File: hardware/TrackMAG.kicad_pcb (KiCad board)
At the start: 4 copper layers, 36 x 36 mm, 54 parts, among them J1 USB_C_Socket_USB2.0, J2 Conn_Debug, SW1 SW_RESET, SW2 SW_BOOT, U1 LSM6DS3TR-C, U2 USBLC6-2P6, U3 STM32F103C8T6, U4 LIS2MDL, U5 AMS1117-3.3, Y1 16MHz

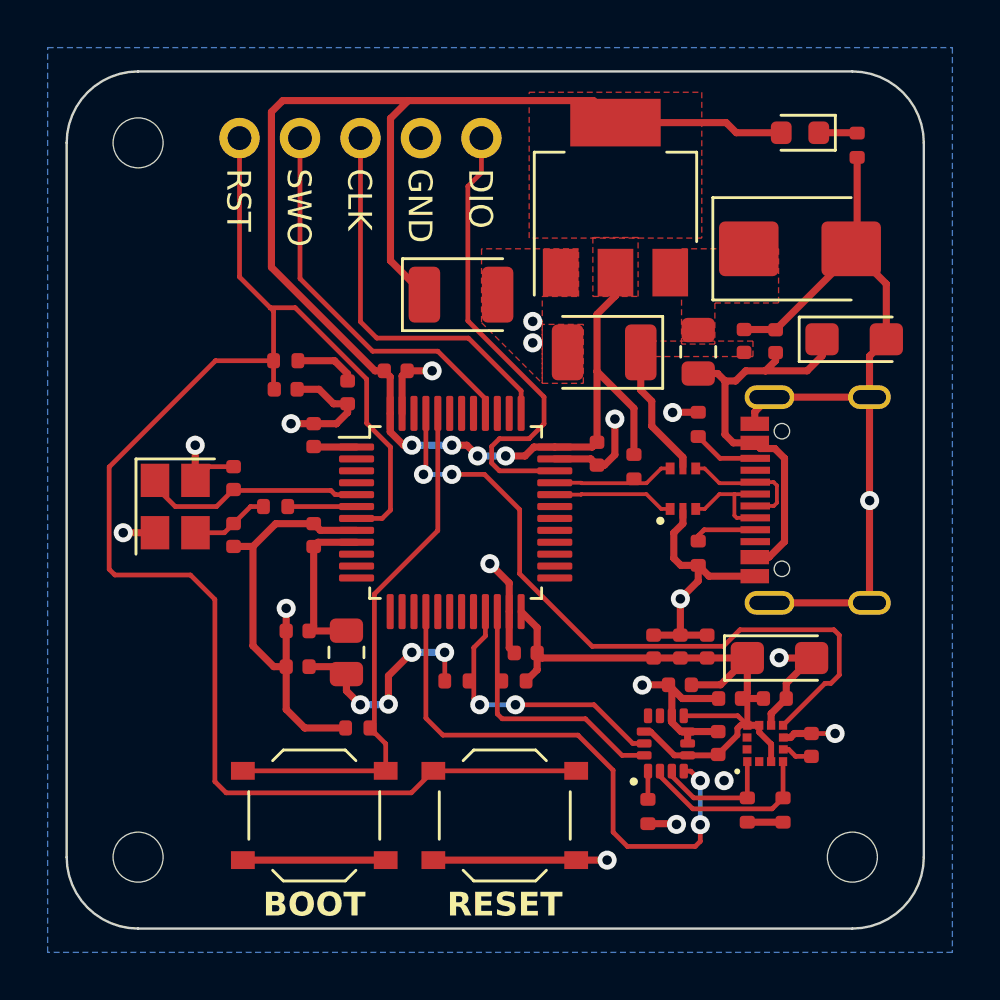
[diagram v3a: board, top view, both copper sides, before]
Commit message: Add ground planes
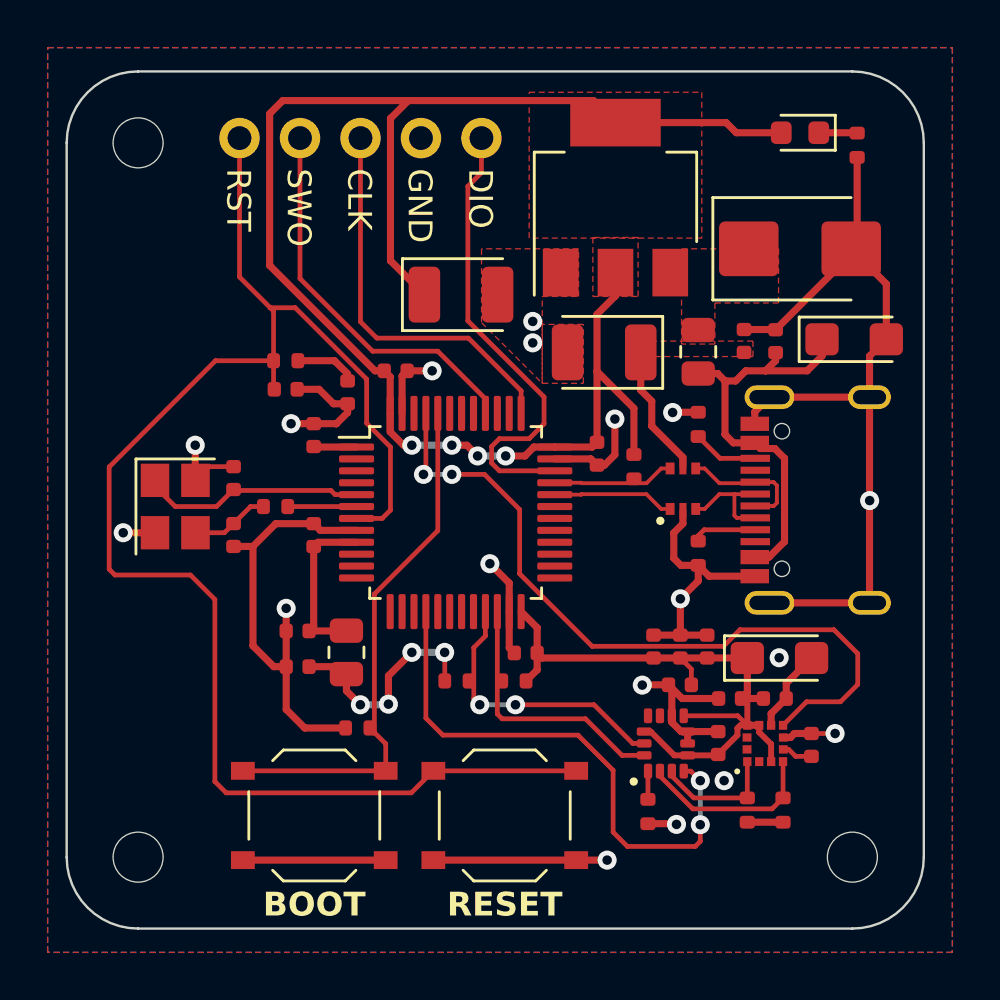
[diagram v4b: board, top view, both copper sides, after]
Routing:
- net +3.3V: track 120.2 -> 118.7 mm
- net GND: track 112.0 -> 110.6 mm
- net DRDY: track 29.9 -> 31.3 mm
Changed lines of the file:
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@@
   (segment (start 51.4 39.95) (end 51.4 33.975) (width 0.3) (layer "F.Cu") (net 1))
   (segment (start 62.45 56.635) (end 57.77 56.635) (width 0.3) (layer "F.Cu") (net 1))
-  (segment (start 46.4 40.225) (end 46.4 33.7) (width 0.3) (layer "F.Cu") (net 1))
-  (segment (start 51.14 44.575) (end 50.75 44.575) (width 0.3) (layer "F.Cu") (net 1))
+  (segment (start 50.75 44.575) (end 51.14 44.575) (width 0.3) (layer "F.Cu") (net 1))
+  (segment (start 64.0375 57.0975) (end 63.575 56.635) (width 0.2) (layer "F.Cu") (net 1))
   (segment (start 49.05 44.15) (end 47.51 44.15) (width 0.3) (layer "F.Cu") (net 1))
   (segment (start 51.3875 44.8225) (end 51.14 44.575) (width 0.3) (layer "F.Cu") (net 1))
@@
   (segment (start 66.095 59.4625) (end 66.3875 59.4625) (width 0.25) (layer "F.Cu") (net 1))
   (segment (start 53.68 57.6) (end 53.68 56.405) (width 0.2) (layer "F.Cu") (net 1))
-  (segment (start 46.875 33.225) (end 52.15 33.225) (width 0.3) (layer "F.Cu") (net 1))
+  (segment (start 52.15 33.225) (end 46.875 33.225) (width 0.3) (layer "F.Cu") (net 1))
   (segment (start 65.9875 59.0625) (end 66.3875 59.4625) (width 0.2) (layer "F.Cu") (net 1))
   (segment (start 58.3 47.775) (end 57.425 47.775) (width 0.3) (layer "F.Cu") (net 1))
   (segment (start 61.625 46.15) (end 60.075 44.6) (width 0.3) (layer "F.Cu") (net 1))
+  (segment (start 46.325 33.775) (end 46.325 40.15) (width 0.3) (layer "F.Cu") (net 1))
   (segment (start 63.325 60.725) (end 63.88 60.725) (width 0.25) (layer "F.Cu") (net 1))
   (segment (start 55.0605 48.15) (end 54.609841 47.699341) (width 0.3) (layer "F.Cu") (net 1))
@@
   (segment (start 52.296271 47.699305) (end 52.196966 47.6) (width 0.3) (layer "F.Cu") (net 1))
   (segment (start 59.875 47.775) (end 60.075 47.575) (width 0.3) (layer "F.Cu") (net 1))
-  (segment (start 50.75 44.575) (end 46.4 40.225) (width 0.3) (layer "F.Cu") (net 1))
   (segment (start 66.3875 63.5325) (end 67.8875 63.5325) (width 0.3) (layer "F.Cu") (net 1))
   (segment (start 57.56 55.36) (end 56.8875 54.6875) (width 0.3) (layer "F.Cu") (net 1))
@@
   (segment (start 60.075 42.2) (end 60.075 44.6) (width 0.3) (layer "F.Cu") (net 1))
   (segment (start 53.68 56.405) (end 53.675 56.4) (width 0.2) (layer "F.Cu") (net 1))
-  (segment (start 64.0375 57.7625) (end 65.2625 57.7625) (width 0.3) (layer "F.Cu") (net 1))
   (segment (start 57.56 56.425) (end 57.56 57.135) (width 0.3) (layer "F.Cu") (net 1))
   (segment (start 52.825 41.375) (end 51.4 39.95) (width 0.3) (layer "F.Cu") (net 1))
@@
   (segment (start 51.3145 57.3835) (end 52.298 56.4) (width 0.3) (layer "F.Cu") (net 1))
   (segment (start 60.075 44.6) (end 60.075 47.575) (width 0.3) (layer "F.Cu") (net 1))
-  (segment (start 46.4 33.7) (end 46.875 33.225) (width 0.3) (layer "F.Cu") (net 1))
+  (segment (start 64.0375 57.7625) (end 64.0375 57.0975) (width 0.2) (layer "F.Cu") (net 1))
   (segment (start 62.055 59.725) (end 62.325 59.725) (width 0.25) (layer "F.Cu") (net 1))
   (segment (start 48.195 47.775) (end 48.175 47.755) (width 0.3) (layer "F.Cu") (net 1))
   (segment (start 66.3875 59.4625) (end 66.8875 59.4625) (width 0.3) (layer "F.Cu") (net 1))
+  (segment (start 46.875 33.225) (end 46.325 33.775) (width 0.3) (layer "F.Cu") (net 1))
   (segment (start 52.15 33.225) (end 59.925 33.225) (width 0.3) (layer "F.Cu") (net 1))
   (segment (start 63.7175 59.0625) (end 65.9875 59.0625) (width 0.2) (layer "F.Cu") (net 1))
@@
   (segment (start 60.85 40.45) (end 60.85 41.425) (width 0.3) (layer "F.Cu") (net 1))
   (segment (start 57.425 47.775) (end 57.05 48.15) (width 0.3) (layer "F.Cu") (net 1))
+  (segment (start 46.325 40.15) (end 50.75 44.575) (width 0.3) (layer "F.Cu") (net 1))
   (segment (start 49.55 58.0145) (end 50.1355 58.6) (width 0.3) (layer "F.Cu") (net 1))
   (segment (start 57.05 48.15) (end 56.2395 48.15) (width 0.3) (layer "F.Cu") (net 1))
-  (segment (start 65.2625 57.7625) (end 66.3875 56.6375) (width 0.3) (layer "F.Cu") (net 1))
   (segment (start 57.56 56.425) (end 57.56 55.36) (width 0.3) (layer "F.Cu") (net 1))
   (segment (start 49.2375 57) (end 49.55 57.3125) (width 0.3) (layer "F.Cu") (net 1))
@@
   (segment (start 71.52 45.68) (end 71.52 50.02) (width 0.3) (layer "F.Cu") (net 2))
   (segment (start 48.455 51.275) (end 48.175 50.995) (width 0.3) (layer "F.Cu") (net 2))
-  (segment (start 69.0875 56.6375) (end 67.7375 56.6375) (width 0.3) (layer "F.Cu") (net 2))
   (segment (start 66.7 46.8) (end 66.7 46.3) (width 0.3) (layer "F.Cu") (net 2))
   (segment (start 64.325 46.315) (end 63.26 46.315) (width 0.3) (layer "F.Cu") (net 2))
@@
   (segment (start 62.149999 49.755) (end 59.426251 49.755) (width 0.16) (layer "F.Cu") (net 22))
   (segment (start 59.406251 49.775) (end 58.3 49.775) (width 0.16) (layer "F.Cu") (net 22))
-  (segment (start 66.077746 55.45) (end 70.025 55.45) (width 0.2) (layer "F.Cu") (net 46))
-  (segment (start 69.65 57.7) (end 67.8875 59.4625) (width 0.2) (layer "F.Cu") (net 46))
+  (segment (start 55.35 48.925) (end 53.977 48.925) (width 0.2) (layer "F.Cu") (net 46))
+  (segment (start 70.025 55.45) (end 66.077746 55.45) (width 0.2) (layer "F.Cu") (net 46))
+  (segment (start 71.025 56.45) (end 70.025 55.45) (width 0.2) (layer "F.Cu") (net 46))
   (segment (start 52.8875 46.3625) (end 52.8875 48.823) (width 0.2) (layer "F.Cu") (net 46))
-  (segment (start 59.87 56.145) (end 65.382746 56.145) (width 0.2) (layer "F.Cu") (net 46))
-  (segment (start 65.382746 56.145) (end 66.077746 55.45) (width 0.2) (layer "F.Cu") (net 46))
-  (segment (start 56.825 50.4) (end 56.825 53.1) (width 0.2) (layer "F.Cu") (net 46))
-  (segment (start 70.25 55.675) (end 70.25 57.35) (width 0.2) (layer "F.Cu") (net 46))
+  (segment (start 56.825 50.4) (end 55.35 48.925) (width 0.2) (layer "F.Cu") (net 46))
+  (segment (start 67.8875 59.4625) (end 68.875 58.475) (width 0.2) (layer "F.Cu") (net 46))
+  (segment (start 66.077746 55.45) (end 65.382746 56.145) (width 0.2) (layer "F.Cu") (net 46))
+  (segment (start 59.87 56.145) (end 56.825 53.1) (width 0.2) (layer "F.Cu") (net 46))
+  (segment (start 70.3 58.475) (end 71.025 57.75) (width 0.2) (layer "F.Cu") (net 46))
+  (segment (start 65.382746 56.145) (end 59.87 56.145) (width 0.2) (layer "F.Cu") (net 46))
   (segment (start 52.8875 48.823) (end 52.7855 48.925) (width 0.2) (layer "F.Cu") (net 46))
-  (segment (start 69.9 57.7) (end 69.65 57.7) (width 0.2) (layer "F.Cu") (net 46))
-  (segment (start 70.025 55.45) (end 70.25 55.675) (width 0.2) (layer "F.Cu") (net 46))
-  (segment (start 53.977 48.925) (end 55.35 48.925) (width 0.2) (layer "F.Cu") (net 46))
-  (segment (start 70.25 57.35) (end 69.9 57.7) (width 0.2) (layer "F.Cu") (net 46))
-  (segment (start 55.35 48.925) (end 56.825 50.4) (width 0.2) (layer "F.Cu") (net 46))
-  (segment (start 56.825 53.1) (end 59.87 56.145) (width 0.2) (layer "F.Cu") (net 46))
+  (segment (start 56.825 53.1) (end 56.825 50.4) (width 0.2) (layer "F.Cu") (net 46))
+  (segment (start 71.025 57.75) (end 71.025 56.45) (width 0.2) (layer "F.Cu") (net 46))
+  (segment (start 68.875 58.475) (end 70.3 58.475) (width 0.2) (layer "F.Cu") (net 46))
   (via (at 52.7855 48.925) (size 0.8) (drill 0.4) (layers "F.Cu" "B.Cu") (net 46))
   (via (at 53.977 48.925) (size 0.8) (drill 0.4) (layers "F.Cu" "B.Cu") (net 46))
@@
       )
     )
+  )
+  (zone (net 2) (net_name "GND") (layer "F.Cu") (hatch edge 0.5)
+    (priority 1)
+    (connect_pads thru_hole_only (clearance 0.5))
+    (min_thickness 0.3) (filled_areas_thickness no)
+    (fill yes (thermal_gap 0.3) (thermal_bridge_width 0.3))
+    (polygon
+      (pts
+        (xy 37 31)
+        (xy 75 31)
+        (xy 75 69)
+        (xy 37 69)
+      )
+    )

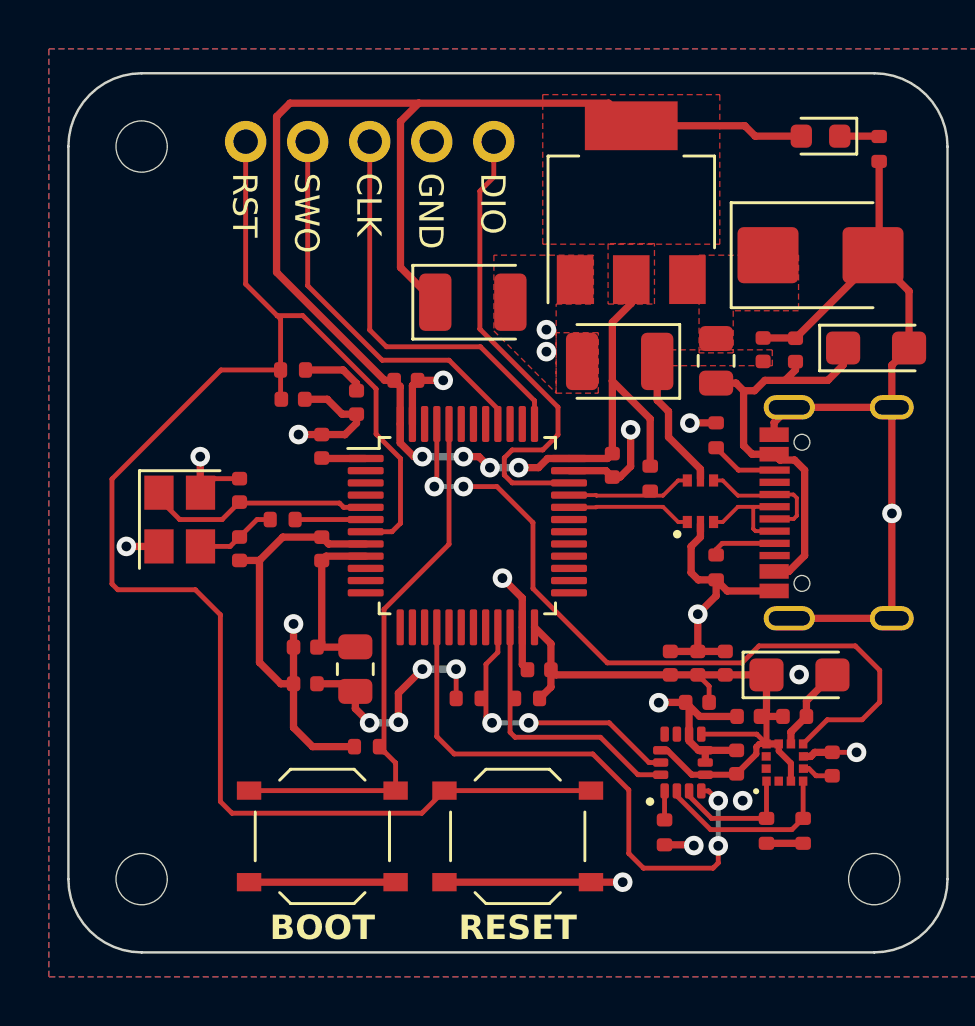
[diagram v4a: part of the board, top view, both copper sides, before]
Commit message: Add missing connections
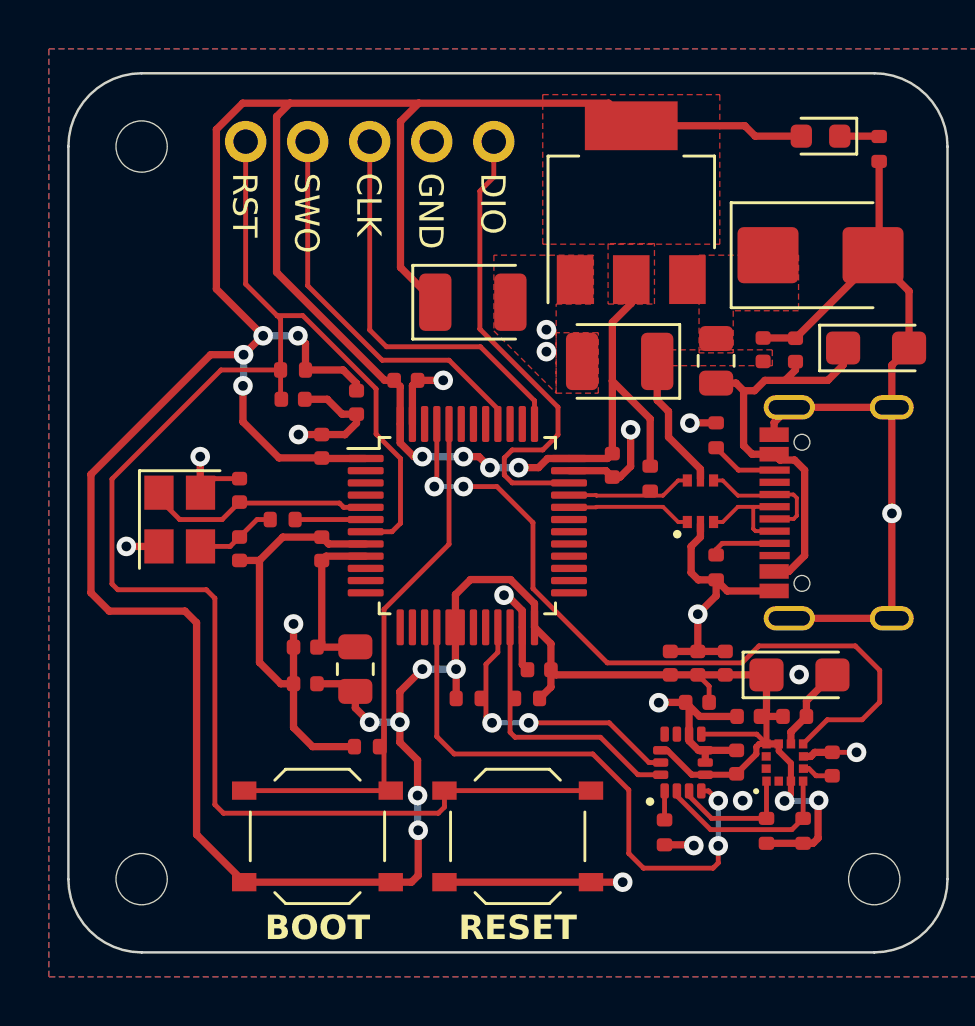
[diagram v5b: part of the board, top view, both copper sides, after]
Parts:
- moved SW2 0.20 mm to (48.0, 63.2)
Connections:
- U3 pad 17: unconnected-(U3-PA7-Pad17) -> +3.3V
- U3 pad 18: unconnected-(U3-PB0-Pad18) -> +3.3V
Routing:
- net +3.3V: track 118.7 -> 191.9 mm, vias 8 -> 16
- net /BOOT0: track 22.6 -> 23.5 mm
- net RESET: track 65.3 -> 66.2 mm
- net GND: track 110.6 -> 110.0 mm

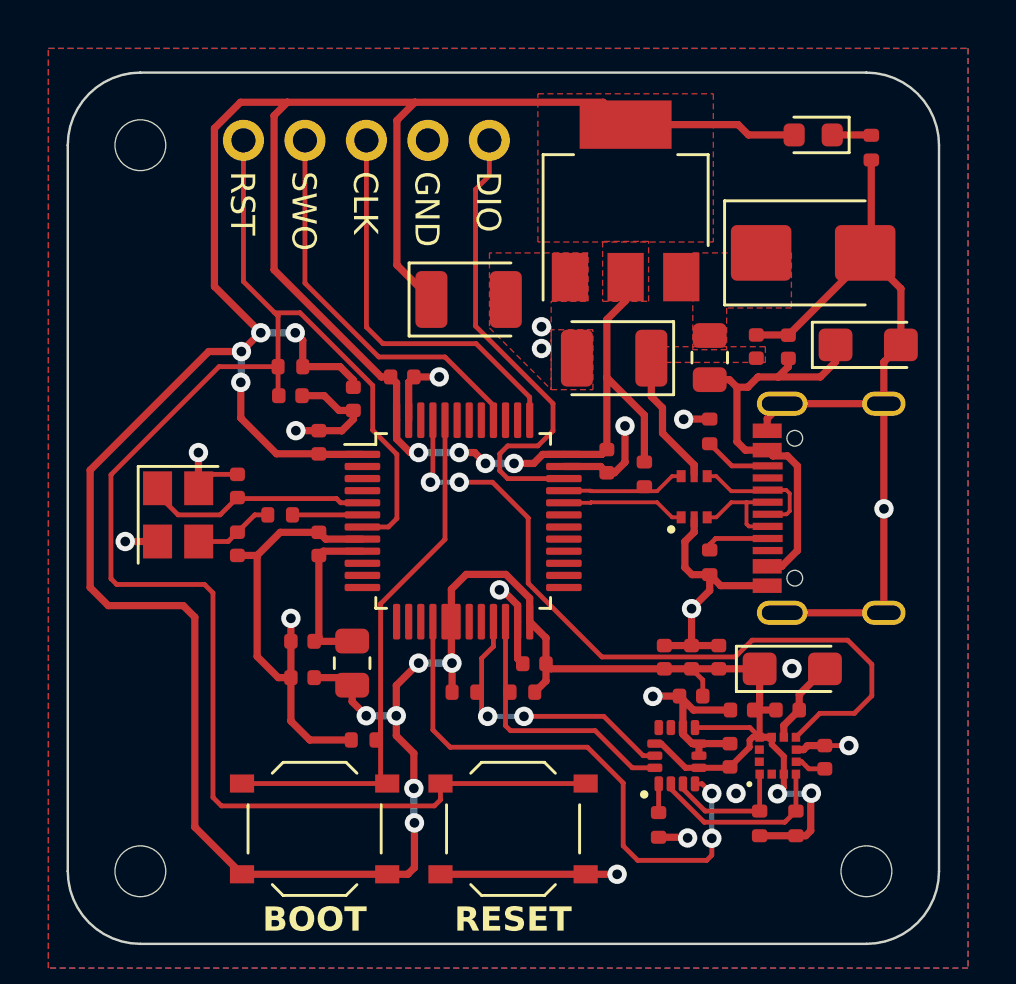
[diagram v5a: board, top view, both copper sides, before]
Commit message: Add reference vias
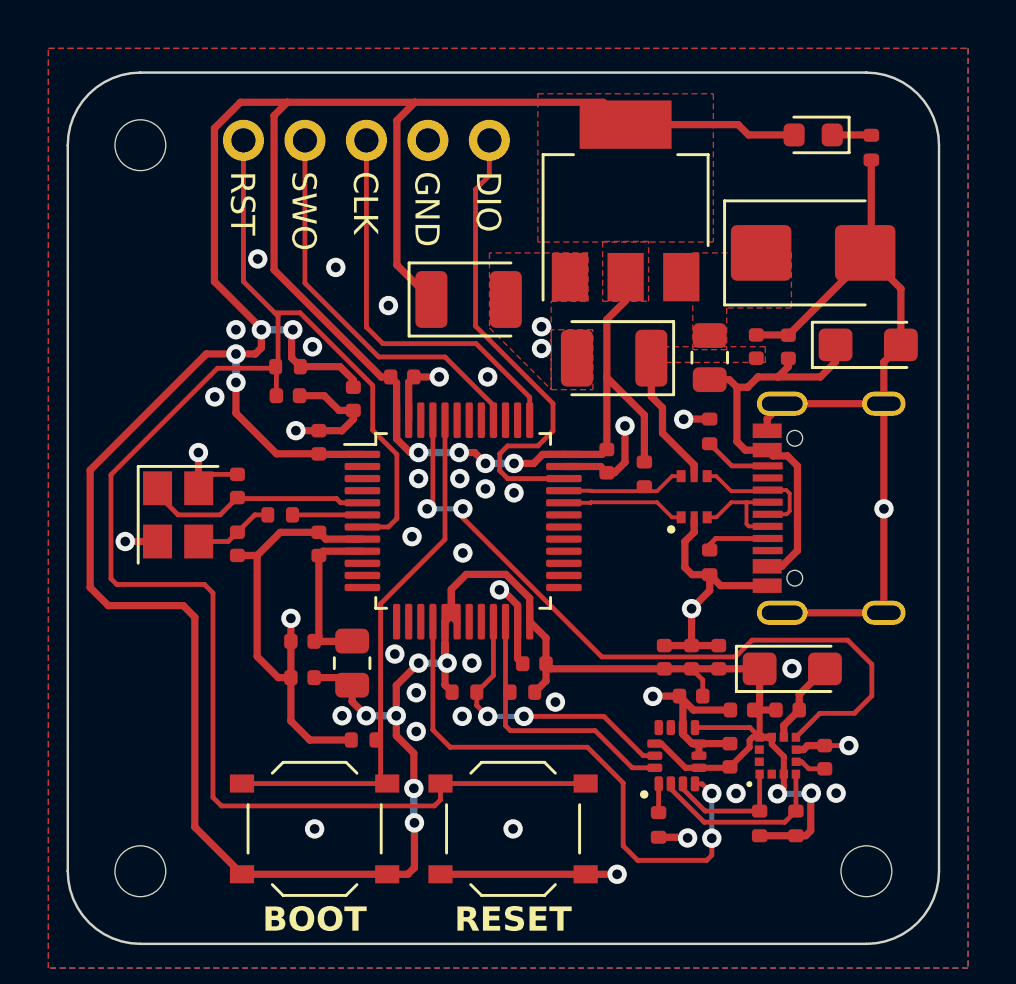
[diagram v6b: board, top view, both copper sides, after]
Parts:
- moved C17 0.10 mm to (46.9, 45.4)
- moved R1 0.10 mm to (46.9, 44.1)
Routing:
- net +3.3V: track 191.9 -> 195.0 mm
- net GND: track 110.0 -> 110.1 mm, vias 18 -> 41
